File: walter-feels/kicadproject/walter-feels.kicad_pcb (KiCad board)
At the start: 4 copper layers, 94 x 94 mm, 153 parts, among them IC1 LTC4015EUHF#PBF, J1 693072010801, J2 1071010, J3 1071010, J4 1990070, J5 1990070, Q1 FDMC8030, Q2 FDMC8327L, Q3 SI7611DN-T1-GE3, Q4 NX7002AK,215, Q5 DMP2021UFDE-7, U1 DPT_Walter, U10 SCD30, U11 LT3120JV#PBF, U12 MAX17291ATA+T, U13 CM1624-08DE, U2 MAX3221, U3 DS9503P+, U4 THVD1450D, U5 SN74LVC1G125DBVR, U6 SN74LVC1G125DBVR, U7 HDC1080DMBR, U8 BMP280, U9 LSM6DSM

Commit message: Updated Walter schematic to v1.5 and updated Walter Feels to version 2.1
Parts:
- U8: value BMP280 -> LPS22HBTR; footprint Package_LGA:Bosch_LGA-8_2x2.5mm_P0.65mm_ClockwisePinNumbering -> LPS22HBTR:HLGA10_2X2_STM-L
- moved U8 1.55 mm to (99.4, 136.5), turned to 90 degrees
- moved C49 0.73 mm to (97.2, 138.6), turned to 180 degrees
- renumbered U9 to locked
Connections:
- U8 pad 1: GND -> +3.3V
- U8 pad 2: +3.3V -> I2C_SCL
- U8 pad 3: I2C_SDA -> GND
- U8 pad 4: I2C_SCL -> I2C_SDA
- U8 pad 7: GND -> unconnected-(U8-Pad7)
- U8 pad 8: +3.3V -> GND
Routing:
- net I2C_SCL: track 92.0 -> 94.8 mm
- net +3.3V: track 148.7 -> 146.7 mm
- net GND: track 40.7 -> 41.8 mm, vias 829 -> 831
- net I2C_SDA: track 94.4 -> 94.2 mm, vias 3 -> 5
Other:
- board text added: "Walter Feels Version 2.1"
- board text added: "WiFi/BLE antenna"
- board text removed: "Walter Feels Version 2.0"

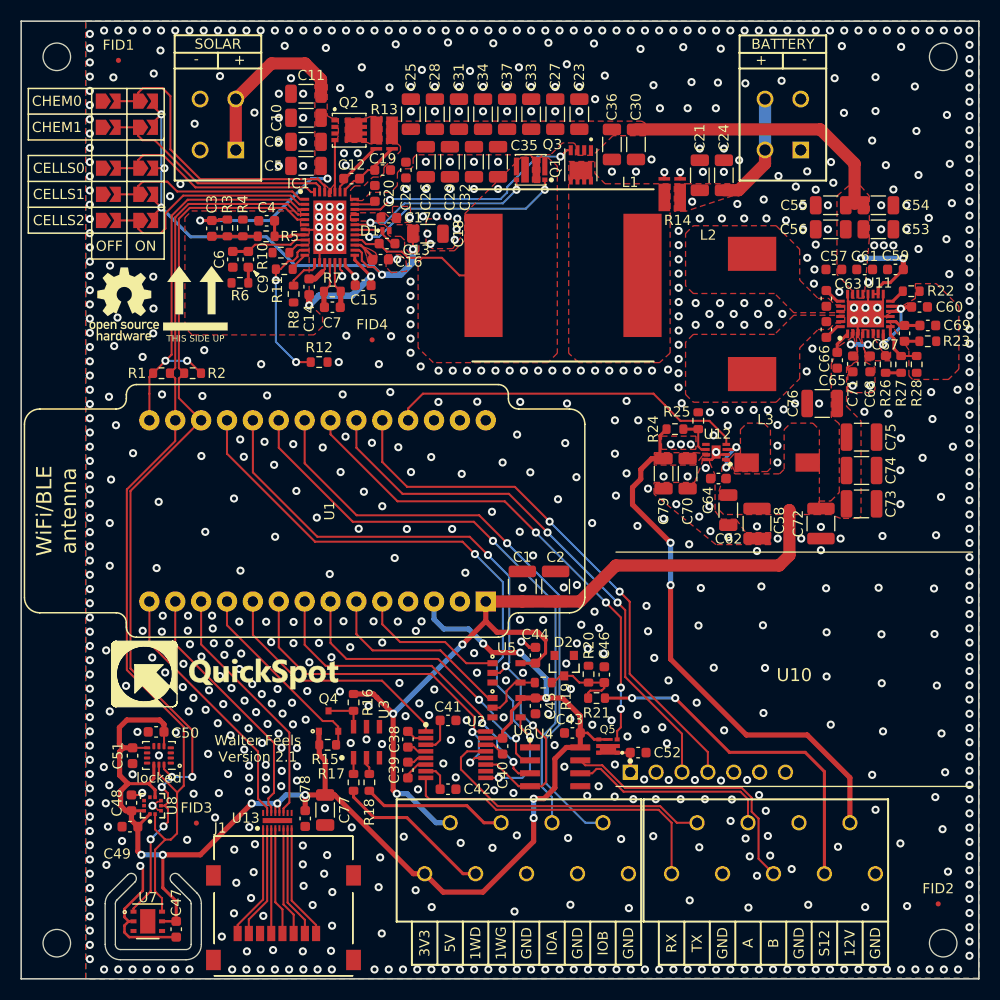
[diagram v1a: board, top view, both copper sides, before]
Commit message: Updated Walter Feels to V2.3
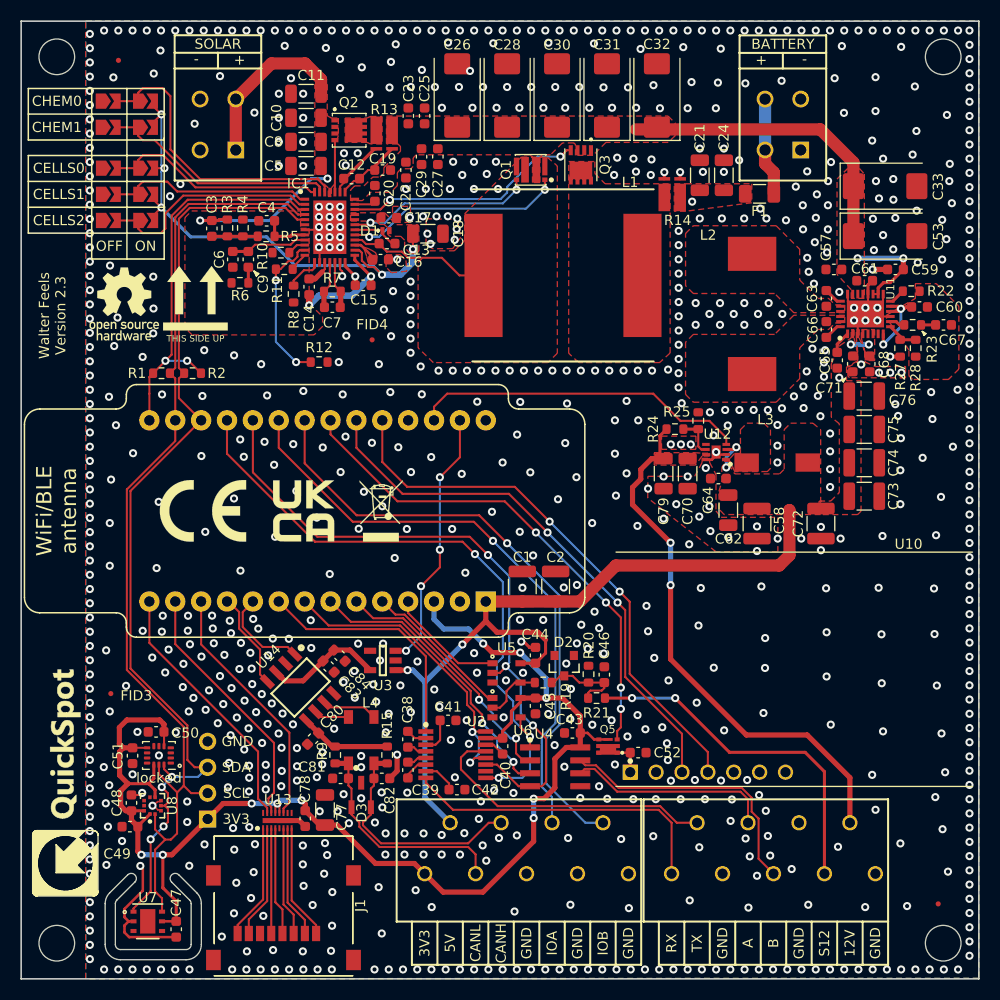
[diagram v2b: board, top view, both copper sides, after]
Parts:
- removed C34, C35, C54, C55, C56: 10µF, Capacitor_SMD:C_1206_3216Metric
- removed C36, C37: 22µF, Capacitor_SMD:C_1206_3216Metric
- removed C69: 27pF, Capacitor_SMD:C_0603_1608Metric
- removed Q4: NX7002AK,215, NX7002AK:TL431CDBZR215
- removed R16: 1.2kΩ 1%, Resistor_SMD:R_0603_1608Metric
- removed R17, R18: 5.1Ω 1%, Resistor_SMD:R_0603_1608Metric
- removed R26: 45.3kΩ 1%, Resistor_SMD:R_0603_1608Metric
- added C80: 4700pF, Capacitor_SMD:C_0603_1608Metric, F.Cu at (115.2, 129.9)
- added C81: 18pF, Capacitor_SMD:C_0603_1608Metric, F.Cu at (117.8, 133.8)
- added C82: 18pF, Capacitor_SMD:C_0603_1608Metric, F.Cu at (121.9, 133.8)
- added C83: 0.1µF, Capacitor_SMD:C_0603_1608Metric, F.Cu at (116.7, 122.8)
- added C84: 10uF, Capacitor_SMD:C_0603_1608Metric, F.Cu at (117.8, 121.8)
- added D3: ESDCAN01-2BLY, ESDCAN01-2BLY:SOT95P255X150-3N, F.Cu at (119.9, 135.4)
- added F1: 5A Slow, Fuse:Fuse_1206_3216Metric, F.Cu at (159.0, 76.5)
- added J6: Conn_01x04_Male, Connector_PinHeader_2.54mm:PinHeader_1x04_P2.54mm_Vertical, F.Cu at (104.8, 137.8)
- added L4: ACT45B-510-2P-TL003, ACT45B-510-2P-TL003:ACT45B1012PTL003, F.Cu at (119.9, 130.1)
- added R9: 60.4Ω, Resistor_SMD:R_0603_1608Metric, F.Cu at (117.3, 131.5)
- added REF**: CE-Logo_8.5x6mm_SilkScreen, Symbol:CE-Logo_8.5x6mm_SilkScreen, F.Cu at (104.3, 107.6)
- added REF**: WEEE-Logo_4.2x6mm_SilkScreen, Symbol:WEEE-Logo_4.2x6mm_SilkScreen, F.Cu at (121.8, 107.6)
- added REF**: UKCA-Logo_6x6mm_SilkScreen, Symbol:UKCA-Logo_6x6mm_SilkScreen, F.Cu at (114.2, 107.6)
- added U14: SN65HVDA1050AQDRQ1, SN65HVDA1050AQDRQ1:SOIC127P600X175-8N, F.Cu at (113.9, 124.9)
- C23, C27: value 22µF -> 1μF; footprint Capacitor_SMD:C_1206_3216Metric -> Capacitor_SMD:C_0603_1608Metric
- C25, C29: value 10µF -> 1μF; footprint Capacitor_SMD:C_1206_3216Metric -> Capacitor_SMD:C_0603_1608Metric
- C26, C28, C31, C32, C53: value 10µF -> 33µF; footprint Capacitor_SMD:C_1206_3216Metric -> Capacitor_Tantalum_SMD:CP_EIA-7343-30_AVX-N
- C30, C33: value 22µF -> 33µF; footprint Capacitor_SMD:C_1206_3216Metric -> Capacitor_Tantalum_SMD:CP_EIA-7343-30_AVX-N
- C63, C66: value 0.1µF -> 0.22µF
- C67: value 150pF -> 1200pF
- R15: value 10kΩ 1% -> 60.4Ω
- R22: value 105kΩ 1% -> 75kΩ 1%
- R23: value 220kΩ 1% -> 64.9kΩ 1%
- R27: value 1.24MΩ 1% -> 1MΩ 1%
- R28: value 243kΩ 1% -> 187kΩ 1%
- U3: value DS9503P+ -> MIC2005A-2YM5-TR; footprint DS9503P+:DS2505PTR -> MIC2005A-2YM5-TR:MIC2005A-2YM5
- U5, U6: value SN74LVC1G125DBVR -> SN74LV1T126DBVR
- moved C33 35.5 mm to (171.3, 75.7), turned to 0 degrees
- moved C32 19.1 mm to (148.9, 66.8), turned to 90 degrees
- moved C23 16.8 mm to (124.5, 68.8), turned to -90 degrees
- moved FID3 15.2 mm to (95.3, 125.5)
- moved C31 14.6 mm to (144.0, 66.8)
- moved C27 12.3 mm to (127.4, 72.8)
- moved C30 9.11 mm to (139.1, 66.8), turned to 90 degrees
- moved U3 8.19 mm to (122.0, 122.2), turned to 180 degrees
- moved C28 7.32 mm to (134.2, 66.8)
- moved C26 7.20 mm to (129.3, 66.8), turned to 90 degrees
- moved R15 5.92 mm to (122.4, 131.5), turned to 90 degrees
- moved C76 4.19 mm to (169.2, 96.3), turned to 0 degrees
- moved C67 3.92 mm to (177.0, 89.3), turned to 0 degrees
- moved C29 2.83 mm to (125.8, 72.8), turned to 90 degrees
- moved R23 2.19 mm to (174.0, 89.3)
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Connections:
- net CO2_EN renamed ~{CO2_EN}
- C23 pad 1: /Power/VIN -> GND
- C23 pad 2: GND -> /Power/VIN
- C25 pad 1: /Power/VIN -> GND
- C25 pad 2: GND -> /Power/VIN
- C27 pad 1: /Power/VIN -> GND
- C27 pad 2: GND -> /Power/VIN
- C29 pad 1: /Power/VIN -> GND
- C29 pad 2: GND -> /Power/VIN
- C67 pad 2: Net-(C67-Pad2) -> GND
- J3 pad 2: VBAT -> Net-(F1-Pad1)
- J5 pad 3: 1W_DAT -> CAN_L
- J5 pad 4: 1W_GND -> CAN_H
- R15 pad 1: +3.3V -> CAN_H
- R15 pad 2: 1W_3V3_IO -> Net-(C80-Pad1)
- R23 pad 1: Net-(C67-Pad2) -> Net-(R23-Pad1)
- R23 pad 2: GND -> Net-(C67-Pad1)
- R27 pad 1: Net-(R26-Pad2) -> +5V
- U1 pad 18: 1W_3V3_IO -> CAN_RX
- U1 pad 19: ~{RS232_RX_EN} -> CAN_TX
- U1 pad 2: unconnected-(U1-Pad2) -> ~{CAN_EN}
- U1 pad 20: RS232_TX_EN -> ~{RS232_RX_EN}
- U1 pad 21: RS485_TX_EN -> RS232_TX_EN
- U1 pad 22: RS485_RX_EN -> RS485_TX_EN
- U1 pad 23: SDI12_RX_EN -> ~{RS485_RX_EN}
- U1 pad 24: SDI12_TX_EN -> SDI12_RX_EN
- U1 pad 25: unconnected-(U1-Pad25) -> SDI12_TX_EN
- U1 pad 3: unconnected-(U1-Pad3) -> 12V_EN
- U1 pad 4: 12V_EN -> unconnected-(U1-Pad4)
- U11 pad 10: Net-(C67-Pad1) -> Net-(R23-Pad1)
- U3 pad 1: Net-(R17-Pad1) -> +5V
- U3 pad 2: Net-(R18-Pad1) -> GND
- U3 pad 3: unconnected-(U3-Pad3) -> ~{CAN_EN}
- U3 pad 5: GND -> Net-(C84-Pad1)
- U4 pad 2: RS485_RX_EN -> ~{RS485_RX_EN}
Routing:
- net RS485_RX_EN: track 29.7 -> 0.00 mm, vias 2 -> 0
- net ~{CAN_EN}: track 0.00 -> 25.8 mm, vias 0 -> 4
- net ~{RS485_RX_EN}: track 0.00 -> 25.1 mm, vias 0 -> 2
- net CAN_H: track 0.00 -> 22.9 mm
- net CAN_L: track 0.00 -> 22.4 mm
- net 1W_3V3_IO: track 19.2 -> 0.00 mm
- net 1W_DAT: track 15.7 -> 0.00 mm
- net 1W_GND: track 14.2 -> 0.00 mm
- net Net-(C84-Pad1): track 0.00 -> 11.6 mm
- net VBAT: track 64.2 -> 52.7 mm
- net Net-(F1-Pad1): track 0.00 -> 9.66 mm
- net CAN_RX: track 0.00 -> 9.60 mm
- net CAN_TX: track 0.00 -> 9.13 mm
- net Net-(C80-Pad1): track 0.00 -> 8.99 mm
- net GND: track 41.8 -> 50.5 mm, vias 831 -> 876
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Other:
- board text added: "CANH"
- board text added: "CANL"
- board text added: "SCL"
- board text added: "SDA"
- board text added: "Walter Feels Version 2.3"
- board text removed: "1WD"
- board text removed: "1WG"
- board text removed: "Walter Feels Version 2.1"

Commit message: Updated to version 2.4
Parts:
- C77: value 10µF -> 4.7μF; footprint Capacitor_SMD:C_1206_3216Metric -> Capacitor_SMD:C_0603_1608Metric
- moved C77 0.93 mm to (115.9, 137.8)
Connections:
- C77 pad 1: +3.3V -> GND
- C77 pad 2: GND -> +3.3V
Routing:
- net GND: vias 876 -> 877
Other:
- board text added: "Walter Feels Version 2.4"
- board text removed: "Walter Feels Version 2.3"

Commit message: Updated Walter Feels project to version 2.6
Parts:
- removed U13: CM1624-08DE, LIB_CM1624-08DE:SON40P135X330X55-17N
- added C34: 10nF, Capacitor_SMD:C_0603_1608Metric, F.Cu at (98.7, 65.5)
- added C35: 10nF, Capacitor_SMD:C_0603_1608Metric, F.Cu at (163.1, 78.4)
- added D4: 8.2V, Diode_SMD:D_SOD-523, F.Cu at (98.3, 64.0)
- added D5: 8.2V, Diode_SMD:D_SOD-523, F.Cu at (163.3, 79.9)
- added D6: D3V3X4U10LP-7, D3V3X4U10LP-7:D3V3X4U10LP7, F.Cu at (111.5, 138.1)
- added F2: 5A Slow, Fuse:Fuse_1206_3216Metric, F.Cu at (159.0, 76.5)
- added Q4: CSD17318Q2, footprints:CSD17318Q2, F.Cu at (163.1, 76.5)
- added Q6: CSD17318Q2, footprints:CSD17318Q2, F.Cu at (99.0, 62.1)
- added R16: 8.2MΩ, Resistor_SMD:R_0603_1608Metric, F.Cu at (124.5, 101.7)
- added R17: 8.2MΩ, Resistor_SMD:R_0603_1608Metric, F.Cu at (95.7, 65.5)
- added R18: 8.2MΩ, Resistor_SMD:R_0603_1608Metric, F.Cu at (159.3, 78.4)
- added R26: 10kΩ, Resistor_SMD:R_0603_1608Metric, F.Cu at (114.8, 138.1)
- added R29: 10kΩ, Resistor_SMD:R_0603_1608Metric, F.Cu at (114.1, 136.4)
- added R30: 10kΩ, Resistor_SMD:R_0603_1608Metric, F.Cu at (113.4, 134.9)
- added R31: 10kΩ, Resistor_SMD:R_0603_1608Metric, F.Cu at (110.2, 134.9)
- added R32: 10kΩ, Resistor_SMD:R_0603_1608Metric, F.Cu at (109.6, 136.4)
- added R33: 10kΩ, Resistor_SMD:R_0603_1608Metric, F.Cu at (108.5, 138.1)
- C77: value 4.7μF -> 1μF
- C84: value 10uF -> 4.7μF
- moved F1 46.1 mm to (114.5, 64.0), turned to 0 degrees
- moved C78 3.18 mm to (117.1, 136.1), turned to 90 degrees
- moved C77 2.07 mm to (117.9, 138.5), turned to 180 degrees
- moved FID1 1.79 mm to (94.8, 62.1)
- moved JP1 1.33 mm to (98.7, 71.2)
- moved JP2 1.33 mm to (95.0, 71.2)
- moved JP3 1.33 mm to (98.7, 68.7)
- moved JP4 1.33 mm to (95.0, 68.7)
- moved JP5 1.33 mm to (98.7, 80.4)
- moved JP6 1.33 mm to (95.1, 80.4)
- moved JP10 1.33 mm to (95.1, 75.3)
- moved JP7 1.33 mm to (98.7, 77.8)
- moved JP8 1.33 mm to (95.1, 77.8)
- moved JP9 1.33 mm to (98.7, 75.3)
- turned C84 to 135 degrees
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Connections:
- C84 pad 1: Net-(C83-Pad1) -> GND
- C84 pad 2: GND -> Net-(C83-Pad1)
- F1 pad 2: VBAT -> VSOLAR
- J1 pad 3: Net-(J1-Pad3) -> SD_CMD
- J1 pad 4: Net-(J1-Pad4) -> +3.3V
- J1 pad 5: Net-(J1-Pad5) -> SD_CLK
- J1 pad 7: Net-(J1-Pad7) -> SD_DAT0
- J2 pad 1: VSOLAR -> Net-(F1-Pad1)
- J2 pad 2: GND -> Net-(C34-Pad2)
- J3 pad 1: GND -> Net-(C35-Pad2)
- J3 pad 2: Net-(F1-Pad1) -> Net-(F2-Pad1)
- R1 pad 1: I2C_BUSPOW -> I2C_SCL
- R1 pad 2: I2C_SCL -> I2C_BUSPOW
- R2 pad 1: I2C_BUSPOW -> I2C_SDA
- R2 pad 2: I2C_SDA -> I2C_BUSPOW
- U1 pad 1: unconnected-(U1-Pad1) -> SYSPOWER_GOOD
- U1 pad 4: unconnected-(U1-Pad4) -> Net-(R16-Pad2)
- U11 pad 7: unconnected-(U11-Pad7) -> SYSPOWER_GOOD
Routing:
- net SYSPOWER_GOOD: track 0.00 -> 44.0 mm, vias 0 -> 2
- net +3.3V: track 138.6 -> 176.6 mm
- net SD_DAT0: track 25.5 -> 38.0 mm
- net SD_CMD: track 24.6 -> 36.4 mm
- net SD_CLK: track 25.1 -> 36.8 mm
- net Net-(J1-Pad7): track 11.1 -> 0.00 mm
- net Net-(J1-Pad3): track 10.7 -> 0.00 mm
- net Net-(J1-Pad4): track 10.6 -> 0.00 mm
- net Net-(J1-Pad5): track 10.3 -> 0.00 mm
- net Net-(F2-Pad1): track 0.00 -> 9.69 mm
- net VSOLAR: track 33.8 -> 39.2 mm, vias 2 -> 3
- net Net-(C35-Pad1): track 0.00 -> 5.18 mm
- net Net-(C35-Pad2): track 0.00 -> 5.00 mm
- net Net-(C34-Pad1): track 0.00 -> 4.49 mm
- net GND: track 50.5 -> 47.5 mm, vias 877 -> 858
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- added copper zone on F.Cu, net Net-(C34-Pad2)
- added copper zone on F.Cu, net Net-(C35-Pad2)
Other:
- board text added: "Walter Feels Version 2.6"
- board text removed: "Walter Feels Version 2.4"
